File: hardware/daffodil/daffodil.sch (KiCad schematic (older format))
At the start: 8 parts, among them J1 NEIGHBOR1, J2 NEIGHBOR2, J7 BONUS_ROW, P1 GREATFET-PROTO-AREA

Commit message: neighbors: pin header part selection
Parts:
- J1, J2: Description (none) -> CONN RCPT .100\" 40POS DUAL-ROW STACKING GOLD; Manufacturer (none) -> Samtec; Part Number (none) -> SSQ-120-23-G-D
- J7: Description (none) -> CONN RCPT .100\" 20POS SINGLE-ROW STACKING GOLD; Manufacturer (none) -> Samtec; Part Number (none) -> SSQ-120-23-G-S
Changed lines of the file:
@@
 EESchema Schematic File Version 2
-LIBS:daffodil-rescue
 LIBS:power
 LIBS:device
@@
 F 2 "gsg-modules:HEADER-2x20" H 15750 1700 60  0001 C CNN
 F 3 "" H 15750 1700 60  0000 C CNN
+F 4 "Samtec" H 15750 2650 60  0001 C CNN "Manufacturer"
+F 5 "SSQ-120-23-G-D" H 15750 2650 60  0001 C CNN "Part Number"
+F 6 "CONN RCPT .100\" 40POS DUAL-ROW STACKING GOLD" H 15750 2650 60  0001 C CNN "Description"
 	1    15750 2650
 	1    0    0    -1
@@
 F 2 "gsg-modules:HEADER-2x20" H 15750 4300 60  0001 C CNN
 F 3 "" H 15750 4300 60  0000 C CNN
+F 4 "Samtec" H 15750 5250 60  0001 C CNN "Manufacturer"
+F 5 "SSQ-120-23-G-D" H 15750 5250 60  0001 C CNN "Part Number"
+F 6 "CONN RCPT .100\" 40POS DUAL-ROW STACKING GOLD" H 15750 5250 60  0001 C CNN "Description"
 	1    15750 5250
 	1    0    0    -1
@@
 F 2 "gsg-modules:HEADER-1x20" H 15200 7000 60  0001 C CNN
 F 3 "" H 15200 7000 60  0000 C CNN
+F 4 "Samtec" H 15200 7000 60  0001 C CNN "Manufacturer"
+F 5 "SSQ-120-23-G-S" H 15200 7000 60  0001 C CNN "Part Number"
+F 6 "CONN RCPT .100\" 20POS SINGLE-ROW STACKING GOLD" H 15200 7000 60  0001 C CNN "Description"
 	1    15200 7000
 	0    -1   -1   0

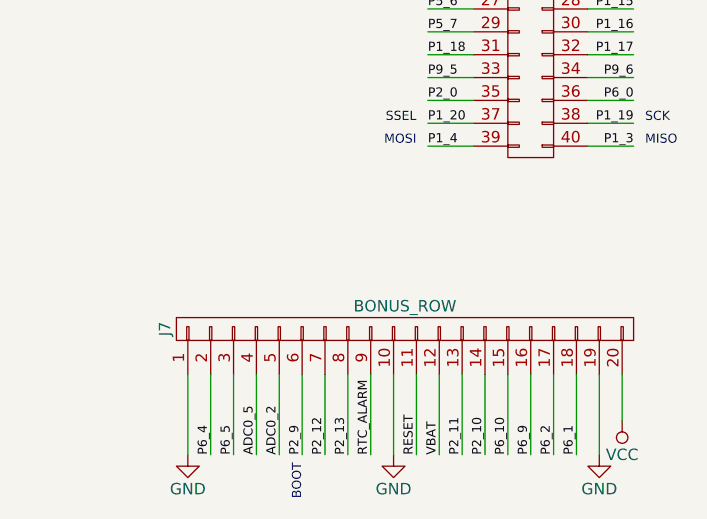
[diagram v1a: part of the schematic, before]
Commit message: neighbors: alternate header selection
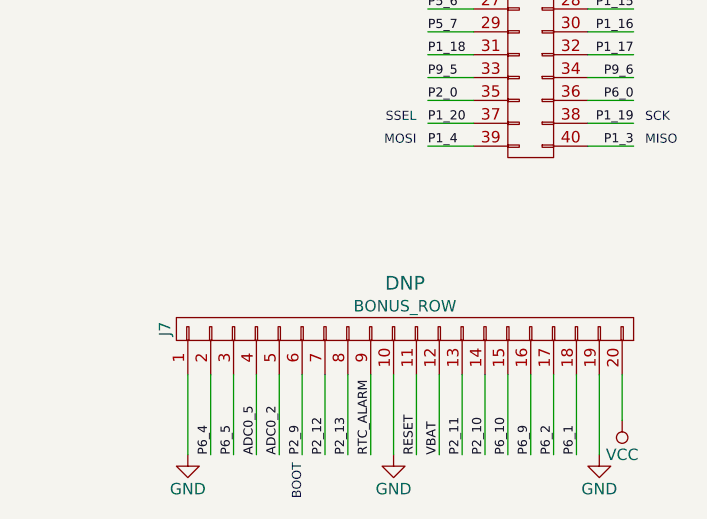
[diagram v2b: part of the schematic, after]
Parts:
- J1, J2: Note (none) -> Alternate: https://www.adafruit.com/products/2223
- J7: Note (none) -> DNP
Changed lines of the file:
@@
 F 5 "SSQ-120-23-G-D" H 15750 2650 60  0001 C CNN "Part Number"
 F 6 "CONN RCPT .100\" 40POS DUAL-ROW STACKING GOLD" H 15750 2650 60  0001 C CNN "Description"
+F 7 "Alternate: https://www.adafruit.com/products/2223" H 15750 2650 60  0001 C CNN "Note"
 	1    15750 2650
 	1    0    0    -1
@@
 F 5 "SSQ-120-23-G-D" H 15750 5250 60  0001 C CNN "Part Number"
 F 6 "CONN RCPT .100\" 40POS DUAL-ROW STACKING GOLD" H 15750 5250 60  0001 C CNN "Description"
+F 7 "Alternate: https://www.adafruit.com/products/2223" H 15750 5250 60  0001 C CNN "Note"
 	1    15750 5250
 	1    0    0    -1
@@
 F 5 "SSQ-120-23-G-S" H 15200 7000 60  0001 C CNN "Part Number"
 F 6 "CONN RCPT .100\" 20POS SINGLE-ROW STACKING GOLD" H 15200 7000 60  0001 C CNN "Description"
+F 7 "DNP" V 15400 7000 60  0000 C CNN "Note"
 	1    15200 7000
 	0    -1   -1   0

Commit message: daffodil: oops, J7 should not be DNP
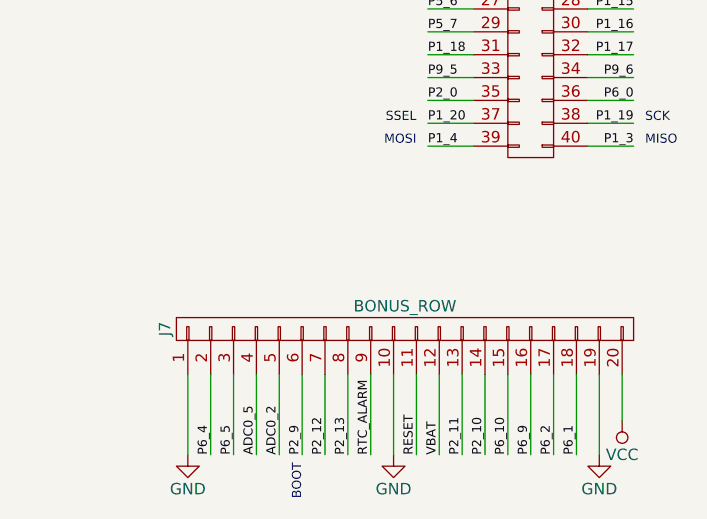
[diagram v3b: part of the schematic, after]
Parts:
- J7: Note DNP -> (none)
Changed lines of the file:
@@
 F 5 "SSQ-120-23-G-S" H 15200 7000 60  0001 C CNN "Part Number"
 F 6 "CONN RCPT .100\" 20POS SINGLE-ROW STACKING GOLD" H 15200 7000 60  0001 C CNN "Description"
-F 7 "DNP" V 15400 7000 60  0000 C CNN "Note"
 	1    15200 7000
 	0    -1   -1   0

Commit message: begonia: designated through-hole prototype area DNP
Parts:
- P1: Note (none) -> DNP
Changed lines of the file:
@@
 F 2 "gsg-modules:GREATFET-PROTO-AREA" H 8350 4700 60  0001 C CNN
 F 3 "" H 8350 4700 60  0000 C CNN
+F 4 "DNP" H 8350 4700 60  0001 C CNN "Note"
 	1    8350 4700
 	1    0    0    -1

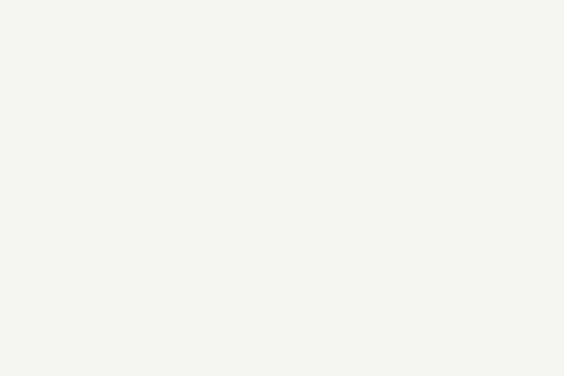
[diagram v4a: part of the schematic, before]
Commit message: daffodil: added solderless breadboard
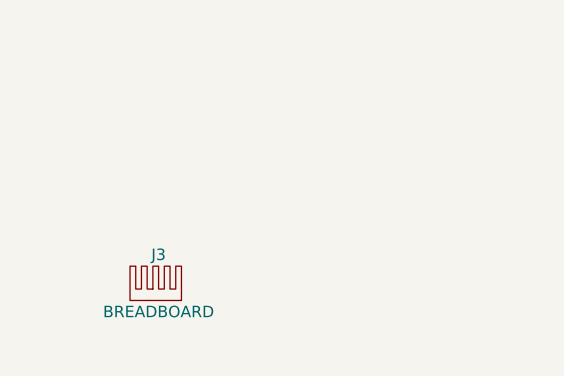
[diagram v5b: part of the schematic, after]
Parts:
- added J3: BREADBOARD, symbol HEATSINK
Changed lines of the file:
@@
+	1    0    0    -1
+$EndComp
+$Comp
+L HEATSINK J3
+U 1 1 569FDCB2
+P 7900 7500
+F 0 "J3" H 7900 7700 50  0000 C CNN
+F 1 "BREADBOARD" H 7900 7450 50  0000 C CNN
+F 2 "" H 7900 7500 60  0000 C CNN
+F 3 "" H 7900 7500 60  0000 C CNN
+F 4 "Parallax" H 7900 7500 60  0001 C CNN "Manufacturer"
+F 5 "700-00012" H 7900 7500 60  0001 C CNN "Part Number"
+F 6 "BREADBOARD SOLDERLESS" H 7900 7500 60  0001 C CNN "Description"
+	1    7900 7500
 	1    0    0    -1
 $EndComp
